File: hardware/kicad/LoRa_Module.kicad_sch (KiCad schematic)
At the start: 3 parts

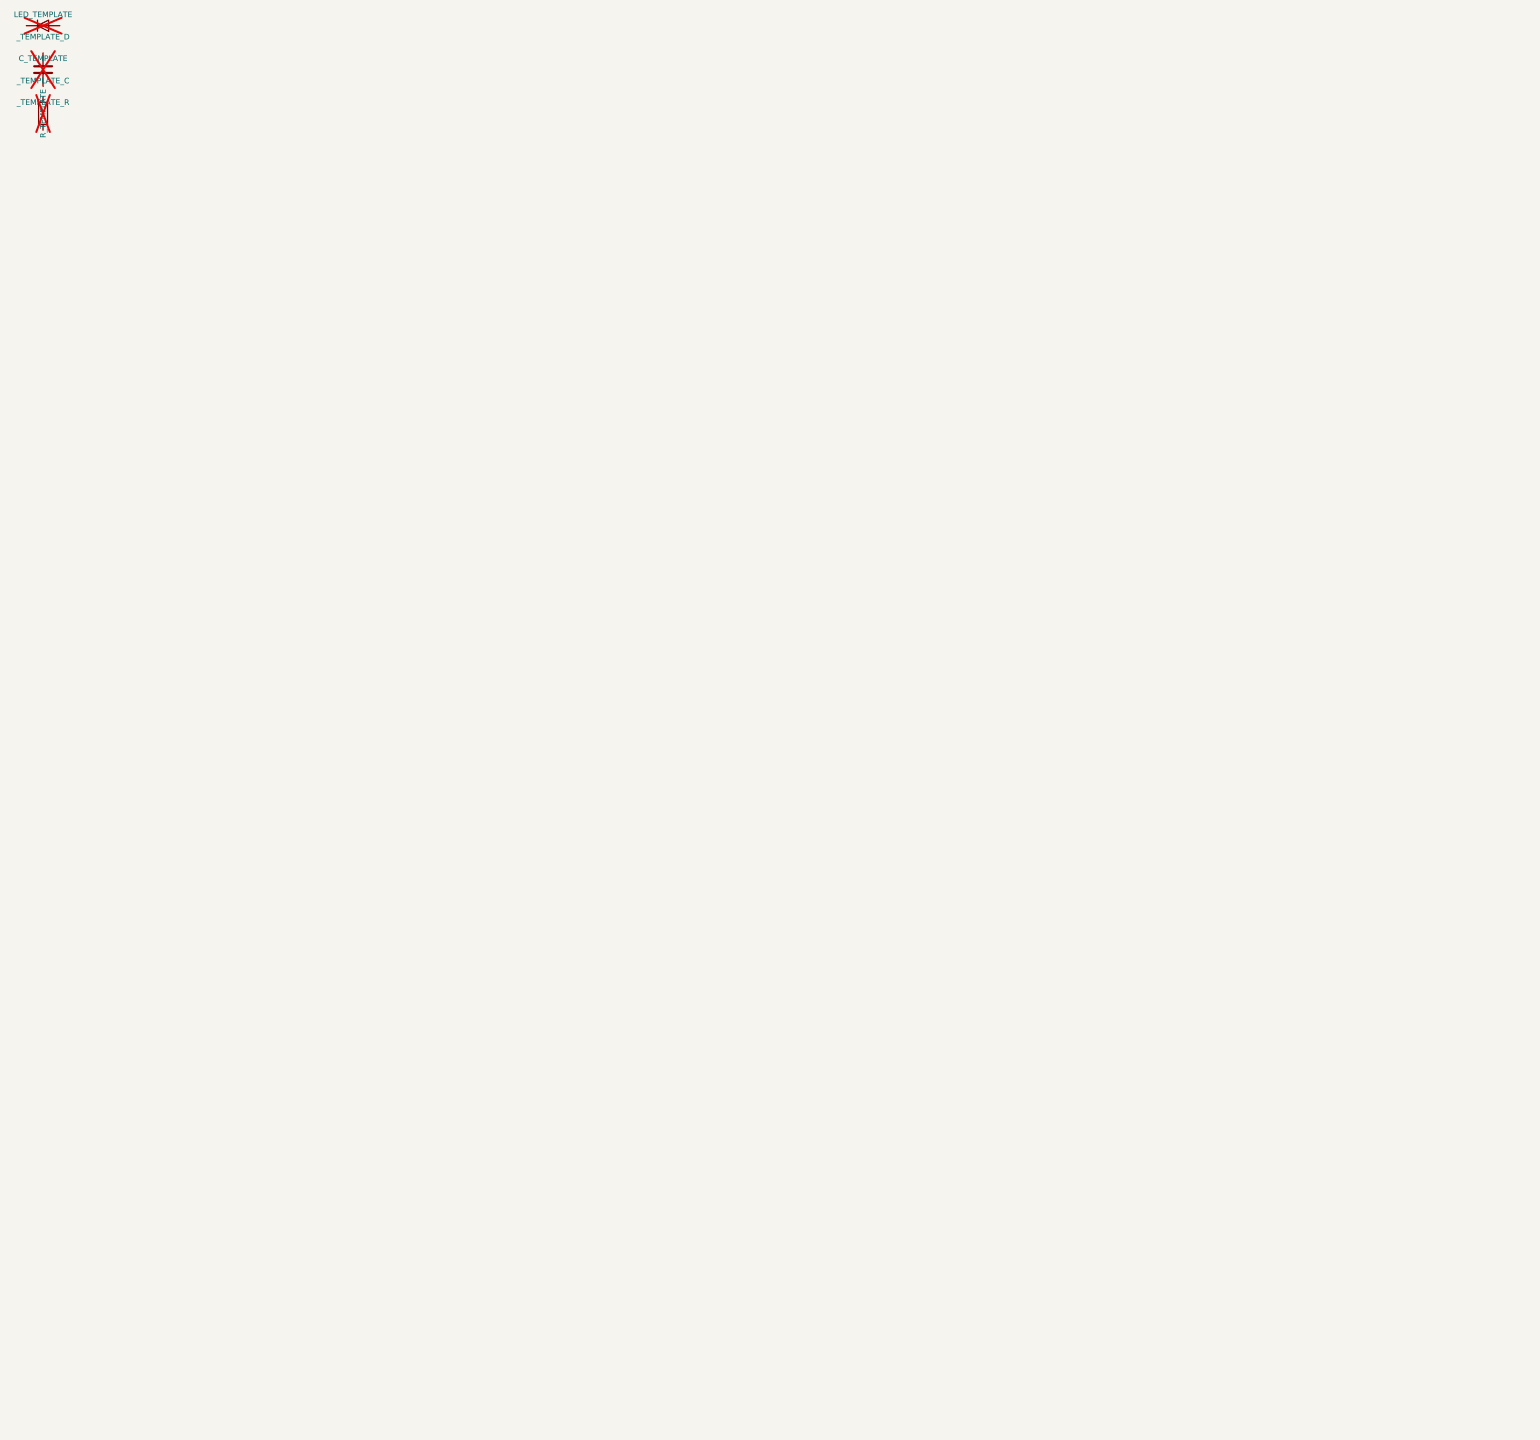
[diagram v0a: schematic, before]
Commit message: Phase A3: hierarchical V1 schematic generated from pstxnet.dat, ERC clean, netlist == pstxnet
gen_symbols.py (R1240N001x, TCAN1042H-Q1, CMS06 diode, VIN_RAW power symbol per current datasheets),
kicad_sym.py (flattened embedding of KiCad 9 library symbols), gen_sch.py (7 sub-sheets mirroring the OrCAD
blocks, labels/hierarchical pins/power symbols, deterministic symbol paths shared with the PCB via v1_design.py),
check_netlist.py (schematic and board nets == pstxnet.dat, refs and footprint paths match).
ERC 0 violations with --severity-all. Allegro refdes without a trailing digit get a '1' suffix (KiCad annotation
rule); original kept in the Allegro_RefDes property.

Co-Authored-By: Claude Fable 5.1 <noreply@anthropic.com>
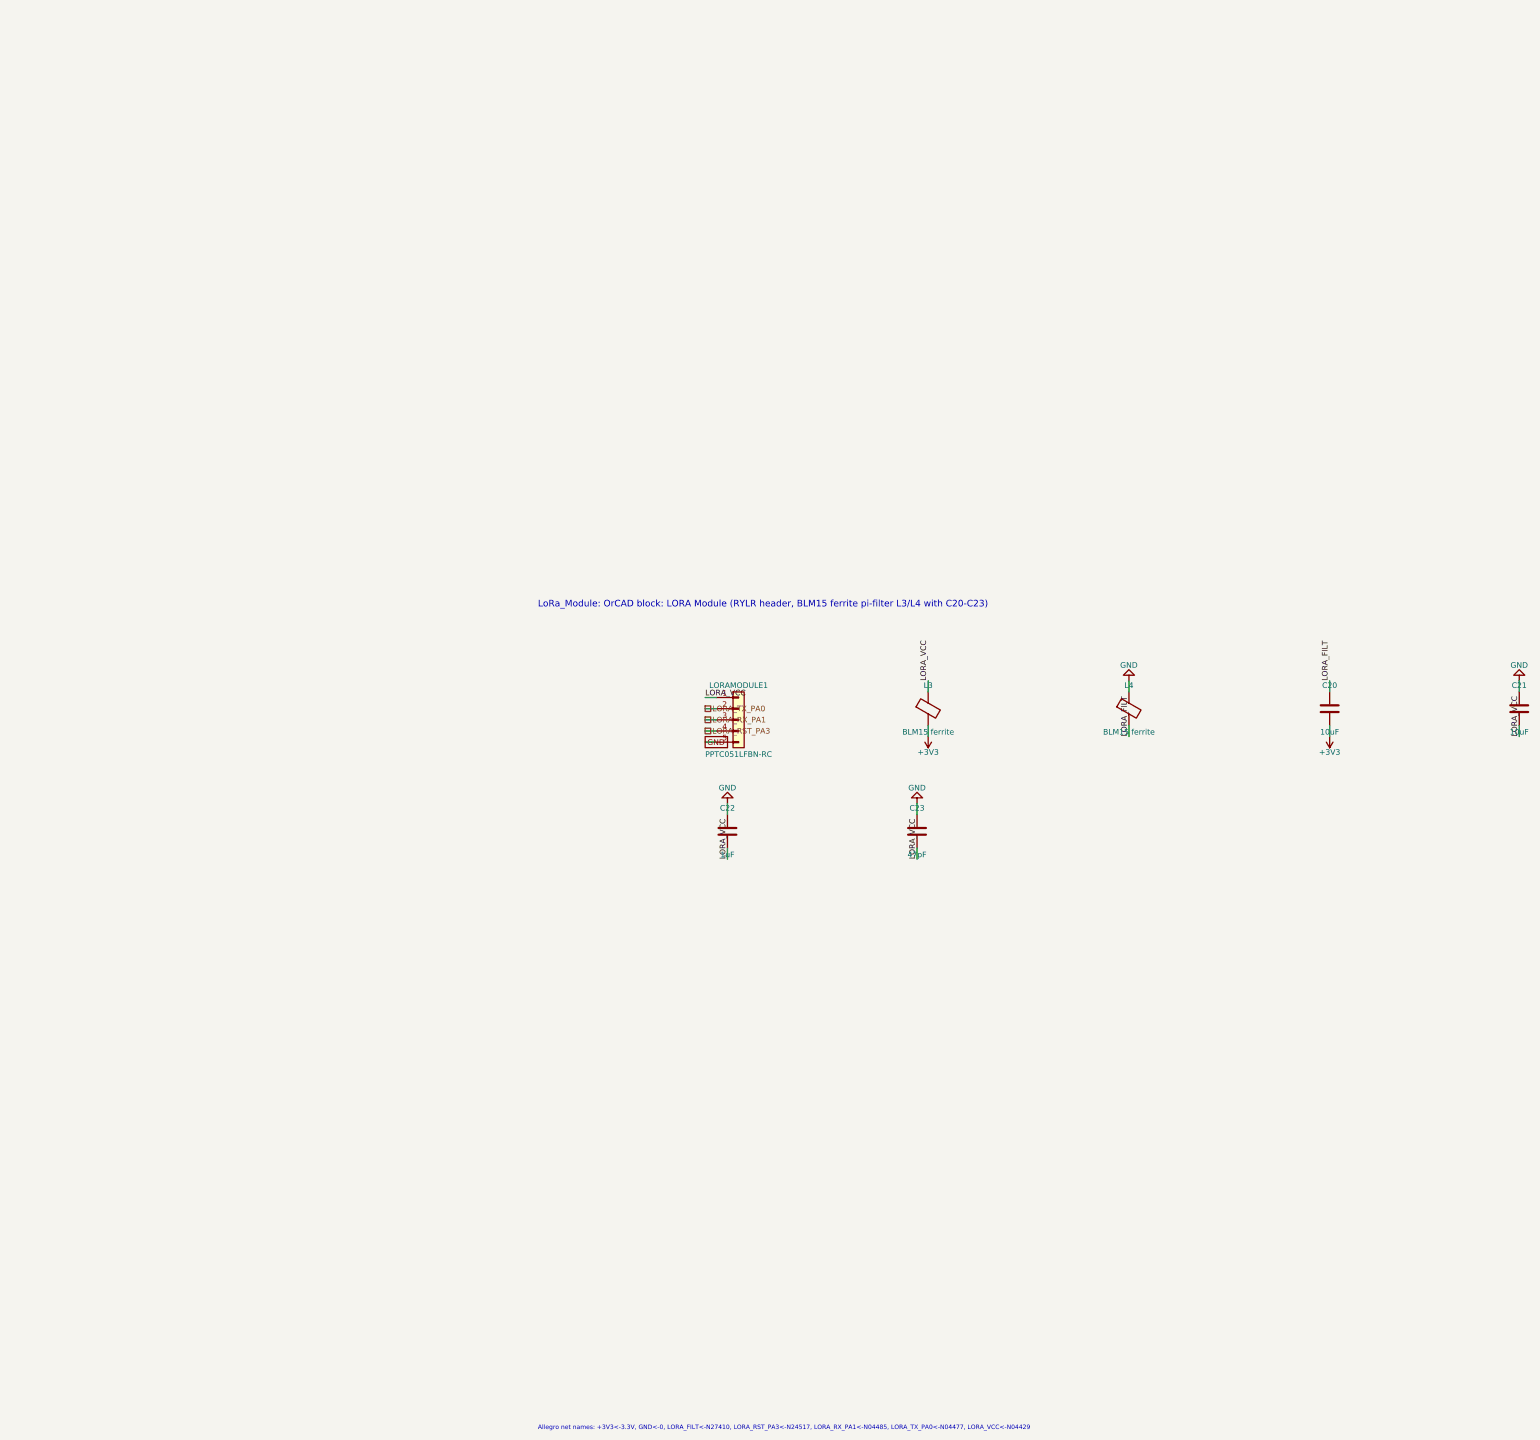
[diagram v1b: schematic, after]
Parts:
- removed _TEMPLATE_C: C_TEMPLATE, symbol Device:C
- removed _TEMPLATE_D: LED_TEMPLATE, symbol Device:LED
- removed _TEMPLATE_R: R_TEMPLATE, symbol Device:R
- added C20, C21: 10uF, LoRa_Boat_Controller:G-21_MUR-L, symbol Device:C
- added C22: 1uF, LoRa_Boat_Controller:CAP_KGM21_KAV-L, symbol Device:C
- added C23: 47pF, LoRa_Boat_Controller:CAP_GJM1555C1H220JB01__MUR-L, symbol Device:C
- added L3, L4: BLM15 ferrite, LoRa_Boat_Controller:IND_BLM15_0402_MUR-L, symbol Device:FerriteBead
- added LORAMODULE1: PPTC051LFBN-RC, LoRa_Boat_Controller:CONN5_1LFBN-RC_SUL, symbol Connector_Generic:Conn_01x05
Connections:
- new net +3V3: C20.2, L3.2
- new net GND: C21.1, C22.1, C23.1, L4.1, LORAMODULE1.5 (Pin_5)
- new net LORA_FILT: C20.1, L4.2
- new net LORA_RST_PA3: LORAMODULE1.4 (Pin_4)
- new net LORA_RX_PA1: LORAMODULE1.3 (Pin_3)
- new net LORA_TX_PA0: LORAMODULE1.2 (Pin_2)
- new net LORA_VCC: C21.2, C22.2, C23.2, L3.1, LORAMODULE1.1 (Pin_1)
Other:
- note added: "Allegro net names: +3V3<-3.3V, GND<-0, LORA_FILT<-N27410, LORA_RST_PA3<-N24517, LORA_RX_PA1<-N04485, LORA_TX_PA0<-N04477, LORA_VCC<-N04429"
- note added: "LoRa_Module: OrCAD block: LORA Module (RYLR header, BLM15 ferrite pi-filter L3/L4 with C20-C23)"
- company: (none) -> University of Arkansas EECS
- title: (none) -> LoRa Autonomous Boat Controller V1 - LoRa_Module

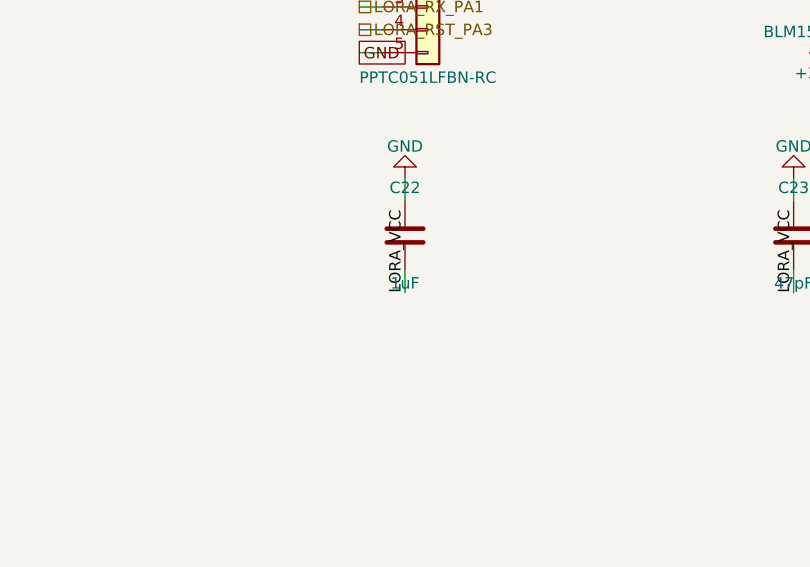
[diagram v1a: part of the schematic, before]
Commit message: Phase A3 close: CANH/CANL net names corrected, BOM with MPNs, DSN-v2 comparison, schematic exports
- gen_pcb.py: N04855 is CANL (U5 pin 6) and N24691 is CANH (U5 pin 7) per pstxnet.dat + TI SLLSES9D; the
  old NETLIST.md had them reversed (Codex review finding R03).
- gen_bom.py: docs/BOM.csv regenerated from the schematic with MPN/manufacturer/description/confidence/price
  columns (research in docs/research/BOM_MPN_RESEARCH.md, prices 2026-09-16).
- a0_xor_dsn.py: DSN v2 copper vs v5 films = 54 % / 63 % mismatch, 0 of 20 vias coincide, 0 of 45 parts unmoved;
  the DSN wiring is unusable for v5 (documented in docs/A0_PROVENANCE.md).
- Schematic PDF and per-sheet SVG exports in docs/img.
Gates: DRC 0 errors / 0 unconnected, ERC 0 violations, netlist check PASS, XOR F.Cu 0.87 % B.Cu 0.23 %.

Co-Authored-By: Claude Fable 5.1 <noreply@anthropic.com>
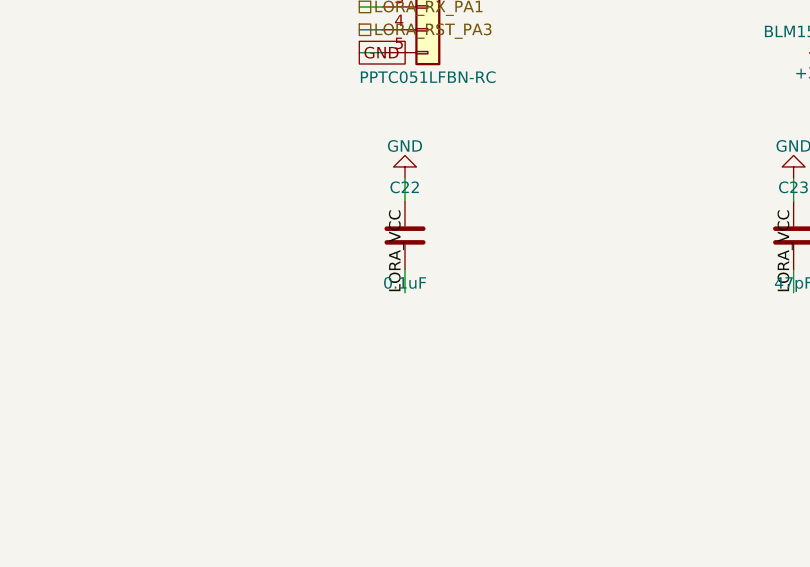
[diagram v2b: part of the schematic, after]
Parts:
- C20, C21: MPN (none) -> GRM21BR61C106KE15L; Manufacturer (none) -> Murata
- C22: value 1uF -> 0.1uF; MPN (none) -> KGM21NR71H104KT; Manufacturer (none) -> Kyocera AVX
- C23: MPN (none) -> GJM1555C1H220JB01D; Manufacturer (none) -> Murata
- L3, L4: MPN (none) -> BLM15AG601SN1D; Manufacturer (none) -> Murata
- LORAMODULE1: MPN (none) -> PPTC051LFBN-RC; Manufacturer (none) -> Sullins Connector Solutions
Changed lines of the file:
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@@
 			)
 		)
-		(property "Description" "Generic connector, single row, 01x05, script generated (kicad-library-utils/schlib/autogen/connector/)"
+		(property "Description" "1x5 2.54 mm female header, through-hole"
 			(at 58.42 38.1 0)
 			(effects
@@
 		)
 		(property "Allegro_Device" "PPTC051LFBN-RC_CONN5_1LFBN-RC_SUL_CONN5_1LFBN-RC"
+			(at 58.42 38.1 0)
+			(effects
+				(font
+					(size 1.27 1.27)
+				)
+				(hide yes)
+			)
+		)
+		(property "MPN" "PPTC051LFBN-RC"
+			(at 58.42 38.1 0)
+			(effects
+				(font
+					(size 1.27 1.27)
+				)
+				(hide yes)
+			)
+		)
+		(property "Manufacturer" "Sullins Connector Solutions"
 			(at 58.42 38.1 0)
 			(effects
@@
 			)
 		)
-		(property "Description" "Ferrite bead"
+		(property "Description" "Ferrite bead 600 ohm @100 MHz 300 mA 0402 - value not specified in the design (typical pick)"
 			(at 101.6 35.56 0)
 			(effects
@@
 		)
 		(property "Allegro_Device" "INDUCTOR_IND_BLM15_0402_MUR-L_INDUCTOR"
+			(at 101.6 35.56 0)
+			(effects
+				(font
+					(size 1.27 1.27)
+				)
+				(hide yes)
+			)
+		)
+		(property "MPN" "BLM15AG601SN1D"
+			(at 101.6 35.56 0)
+			(effects
+				(font
+					(size 1.27 1.27)
+				)
+				(hide yes)
+			)
+		)
+		(property "Manufacturer" "Murata"
 			(at 101.6 35.56 0)
 			(effects
@@
 			)
 		)
-		(property "Description" "Ferrite bead"
+		(property "Description" "Ferrite bead 600 ohm @100 MHz 300 mA 0402 - value not specified in the design (typical pick)"
 			(at 147.32 35.56 0)
 			(effects
@@
 		)
 		(property "Allegro_Device" "INDUCTOR_IND_BLM15_0402_MUR-L_INDUCTOR"
+			(at 147.32 35.56 0)
+			(effects
+				(font
+					(size 1.27 1.27)
+				)
+				(hide yes)
+			)
+		)
+		(property "MPN" "BLM15AG601SN1D"
+			(at 147.32 35.56 0)
+			(effects
+				(font
+					(size 1.27 1.27)
+				)
+				(hide yes)
+			)
+		)
+		(property "Manufacturer" "Murata"
 			(at 147.32 35.56 0)
 			(effects
@@
 			)
 		)
-		(property "Description" "Unpolarized capacitor"
+		(property "Description" "10 uF 10% 16 V X5R MLCC 0805 (design gives GRM21 only)"
 			(at 193.04 35.56 0)
 			(effects
@@
 		)
 		(property "Allegro_Device" "C_G-21_MUR-L_10UF"
+			(at 193.04 35.56 0)
+			(effects
+				(font
+					(size 1.27 1.27)
+				)
+				(hide yes)
+			)
+		)
+		(property "MPN" "GRM21BR61C106KE15L"
+			(at 193.04 35.56 0)
+			(effects
+				(font
+					(size 1.27 1.27)
+				)
+				(hide yes)
+			)
+		)
+		(property "Manufacturer" "Murata"
 			(at 193.04 35.56 0)
 			(effects
@@
 			)
 		)
-		(property "Description" "Unpolarized capacitor"
+		(property "Description" "10 uF 10% 16 V X5R MLCC 0805 (design gives GRM21 only)"
 			(at 236.22 35.56 0)
 			(effects
@@
 		)
 		(property "Allegro_Device" "C_G-21_MUR-L_10UF"
+			(at 236.22 35.56 0)
+			(effects
+				(font
+					(size 1.27 1.27)
+				)
+				(hide yes)
+			)
+		)
+		(property "MPN" "GRM21BR61C106KE15L"
+			(at 236.22 35.56 0)
+			(effects
+				(font
+					(size 1.27 1.27)
+				)
+				(hide yes)
+			)
+		)
+		(property "Manufacturer" "Murata"
 			(at 236.22 35.56 0)
 			(effects
@@
 			)
 		)
-		(property "Value" "1uF"
+		(property "Value" "0.1uF"
 			(at 55.88 68.81 0)
 			(effects
@@
 			)
 		)
-		(property "Description" "Unpolarized capacitor"
+		(property "Description" "0.1 uF 10% 50 V X7R MLCC 0805"
 			(at 55.88 63.5 0)
 			(effects
@@
 		)
 		(property "Allegro_Device" "C_CAP_KGM21_KAV-L_.1UF"
+			(at 55.88 63.5 0)
+			(effects
+				(font
+					(size 1.27 1.27)
+				)
+				(hide yes)
+			)
+		)
+		(property "MPN" "KGM21NR71H104KT"
+			(at 55.88 63.5 0)
+			(effects
+				(font
+					(size 1.27 1.27)
+				)
+				(hide yes)
+			)
+		)
+		(property "Manufacturer" "Kyocera AVX"
 			(at 55.88 63.5 0)
 			(effects
@@
 			)
 		)
-		(property "Description" "Unpolarized capacitor"
+		(property "Description" "22 pF 5% 50 V C0G MLCC 0402 - NOTE: device name encodes 22 pF, schematic value says 47 pF (GJM1555C1H470JB01D); resolve"
 			(at 99.06 63.5 0)
 			(effects
@@
 			(at 99.06 63.5 0)
 			(effects
+				(font
+					(size 1.27 1.27)
+				)
+				(hide yes)
+			)
+		)
+		(property "MPN" "GJM1555C1H220JB01D"
+			(at 99.06 63.5 0)
+			(effects
+				(font
+					(size 1.27 1.27)
+				)
+				(hide yes)
+			)
+		)
+		(property "Manufacturer" "Murata"
+			(at 99.06 63.5 0)
+			(effects
